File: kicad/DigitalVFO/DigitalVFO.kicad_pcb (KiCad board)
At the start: 2 copper layers, 86.1 x 56.5 mm, 41 parts, among them J1 Coax, J2 Conn_01x03, Q1 2N2222A, SW1 Rotary_Encoder_Switch, U1 74HC14, U2 Teensy3.2, U3 LCD1602A, U4 DDS-60

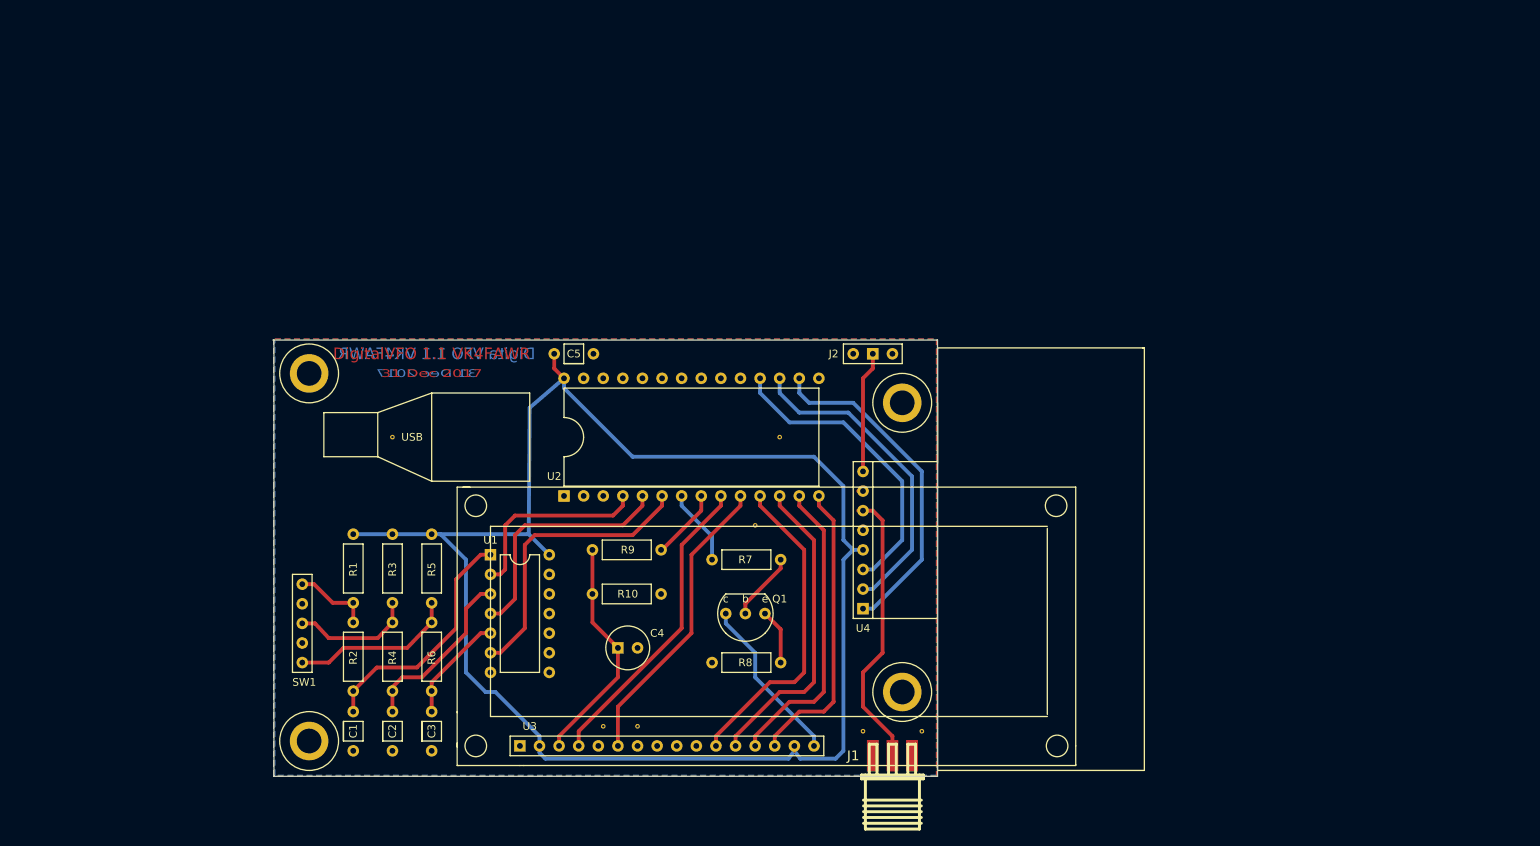
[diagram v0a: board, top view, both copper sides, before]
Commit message: Changing footprints and smaller board
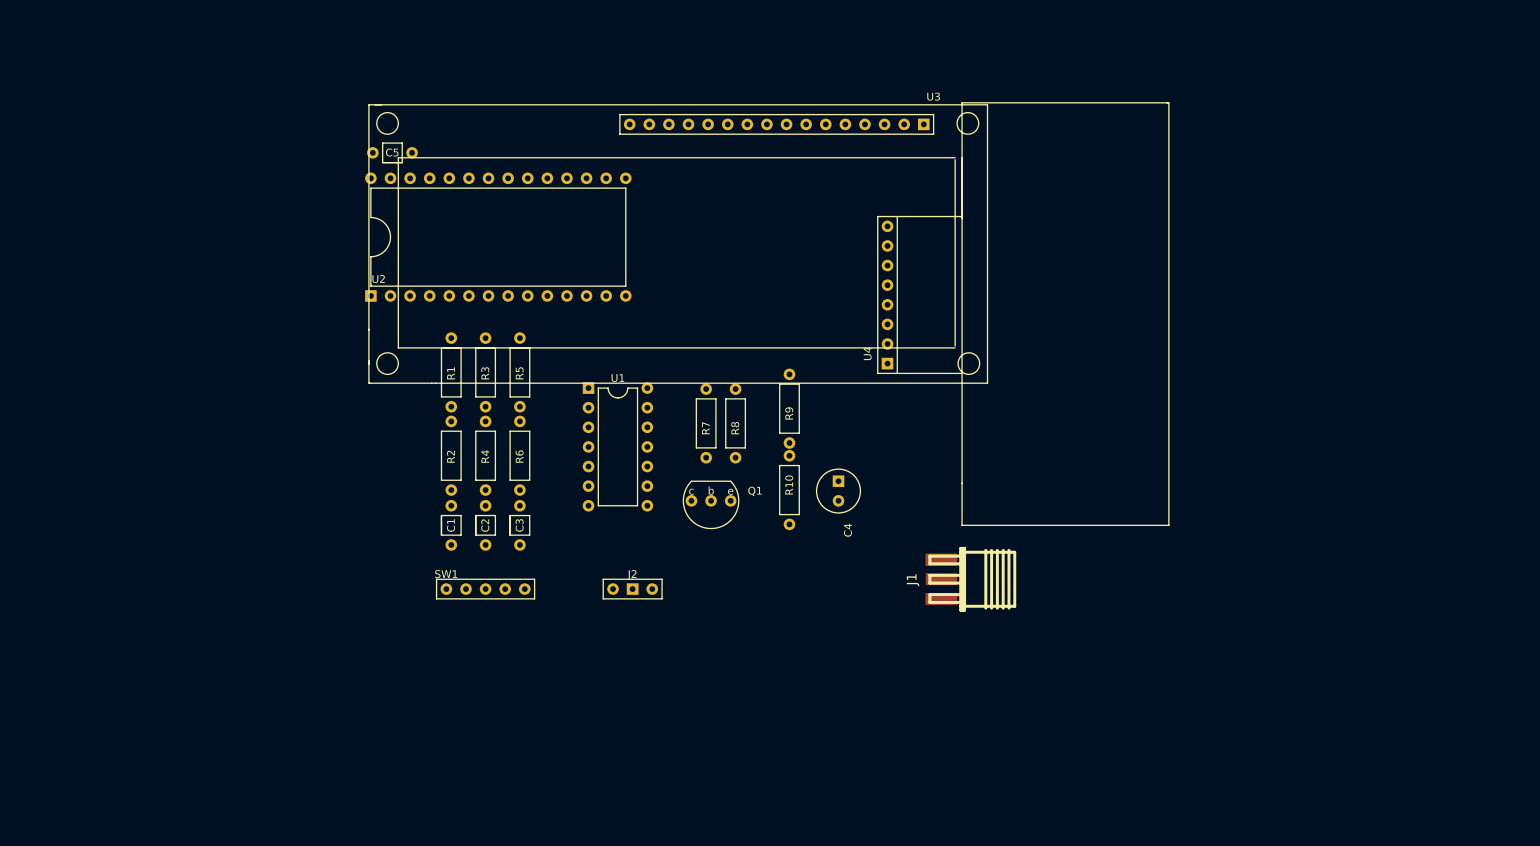
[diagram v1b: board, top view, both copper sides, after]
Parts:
- removed REF** (x14): Via-0.6mm, teensy:Via-0.6mm
- removed REF** (x4): Conn_Mount, teensy:Conn_Mount
- moved U3 50.8 mm to (135.9, 64.1)
- moved J2 43.6 mm to (142.9, 93.3)
- moved C4 35.8 mm to (169.5, 79.4), turned to 270 degrees
- moved U2 35.5 mm to (126.4, 47.6), turned to 0 degrees
- moved C5 35.1 mm to (109.2, 36.8)
- moved U4 31.9 mm to (175.9, 55.2)
- moved R8 31.1 mm to (156.2, 71.8), turned to 90 degrees
- moved C1 29.5 mm to (119.4, 82.5)
- moved C2 29.3 mm to (123.8, 82.5)
- moved C3 29.0 mm to (128.3, 82.5)
- moved R2 29.0 mm to (119.4, 76.2)
- moved R4 28.7 mm to (123.8, 76.2)
- moved R6 28.4 mm to (128.3, 76.2)
- moved R1 28.4 mm to (119.4, 65.4)
- moved R3 28.1 mm to (123.8, 65.4)
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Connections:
- U2 pad 4: Net-(U1-Pad2) -> Net-(U1-Pad6)
- U2 pad 6: Net-(U1-Pad6) -> Net-(U1-Pad2)
- U3 pad 11: Net-(U2-Pad11) -> Net-(U2-Pad12)
- U3 pad 12: Net-(U2-Pad12) -> Net-(U2-Pad11)
- U3 pad 13: Net-(U2-Pad13) -> Net-(U2-Pad10)
- U3 pad 14: Net-(U2-Pad14) -> Net-(U2-Pad9)
- U3 pad 4: Net-(U2-Pad9) -> Net-(U2-Pad14)
- U3 pad 6: Net-(U2-Pad10) -> Net-(U2-Pad13)
- U4 pad 1: Net-(U2-Pad16) -> Net-(U2-Pad18)
- U4 pad 3: Net-(U2-Pad18) -> Net-(U2-Pad16)
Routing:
- net +5V: track 210.3 -> 0.00 mm
- net Net-(U2-Pad16): track 43.7 -> 0.00 mm
- net Net-(U2-Pad11): track 42.0 -> 0.00 mm
- net Net-(U2-Pad17): track 41.5 -> 0.00 mm
- net Net-(U2-Pad12): track 40.5 -> 0.00 mm
- net Net-(U2-Pad9): track 40.0 -> 0.00 mm
- net Net-(U2-Pad18): track 40.0 -> 0.00 mm
- net Net-(U2-Pad13): track 39.9 -> 0.00 mm
- net Net-(U2-Pad10): track 39.0 -> 0.00 mm
- net Net-(U2-Pad14): track 38.2 -> 0.00 mm
- net Net-(U1-Pad6): track 37.7 -> 0.00 mm
- net Net-(J1-Pad1): track 37.4 -> 0.00 mm
- net Net-(C1-Pad1): track 32.0 -> 0.00 mm
- net Net-(U1-Pad4): track 31.6 -> 0.00 mm
- net Net-(C4-Pad1): track 29.9 -> 0.00 mm
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- removed copper zone on B.Cu, net GND
- removed copper zone on F.Cu, net GND
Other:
- board outline removed
- net class normal removed
- board text removed: "31 Dec 2017"
- board text removed: "DigitalVFO 1.1 VK4FAWR"

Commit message: Working on new PCB
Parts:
- J1: footprint teensy:Conn_SMA_Edge -> Connectors:SMA_THT_Jack_Straight
- moved J1 91.8 mm to (95.9, 69.2), turned to 180 degrees
- moved U4 76.3 mm to (99.7, 50.8), turned to 180 degrees
- moved C5 52.5 mm to (160.0, 50.2), turned to 180 degrees
- moved U3 46.7 mm to (90.2, 54.6)
- moved U1 23.6 mm to (131.4, 53.3), turned to 90 degrees
- moved C3 23.0 mm to (117.5, 62.2)
- moved R5 23.0 mm to (117.5, 45.1)
- moved R6 23.0 mm to (117.5, 55.9)
- moved C1 23.0 mm to (108.6, 62.2)
- moved C2 23.0 mm to (113.0, 62.2)
- moved R1 23.0 mm to (108.6, 45.1)
- moved R2 23.0 mm to (108.6, 55.9)
- moved R3 23.0 mm to (113.0, 45.1)
- moved R4 23.0 mm to (113.0, 55.9)
- moved J2 21.9 mm to (132.1, 74.3)
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
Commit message: Almost ready with v1.2
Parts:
- added C6: 0.1uF, teensy:Cap_SmV, F.Cu at (168.1, 90.9)
- added C7: 0.1uF, teensy:Cap_SmV, F.Cu at (162.6, 106.2)
- added G***: LOGO, teensy:logo, F.Cu at (147.8, 80.8)
- added REF**: Conn_Mount, teensy:Conn_Mount, F.Cu at (235.7, 68.1)
- added REF**: Conn_Mount, teensy:Conn_Mount, F.Cu at (144.3, 68.1)
- added REF**: Conn_Mount, teensy:Conn_Mount, F.Cu at (144.3, 109.7)
- added REF**: Conn_Mount, teensy:Conn_Mount, F.Cu at (219.5, 105.7)
- added REF**: Via-0.6mm, teensy:Via-0.6mm, F.Cu at (234.2, 77.7)
- added STRAP**: Strap_23, teensy:Strap_23, F.Cu at (159.0, 94.0)
- J1: footprint Connectors:SMA_THT_Jack_Straight -> teensy:BNC_Socket
- J2: value Conn_01x03 -> Conn_01x02; footprint teensy:Conn_Power_3 -> teensy:Conn_Power_2
- SW1: footprint teensy:Conn_RE5 -> teensy:Conn_RE_Switch
- moved J1 143.0 mm to (233.7, 107.3), turned to 270 degrees
- moved U2 89.2 mm to (221.0, 81.3)
- moved C5 88.7 mm to (238.3, 91.9)
- moved U3 88.6 mm to (167.6, 97.5)
- moved SW1 85.6 mm to (194.1, 103.6), turned to 0 degrees
- moved R7 82.9 mm to (217.9, 92.5), turned to 0 degrees
- moved R8 81.1 mm to (217.9, 97.0), turned to 0 degrees
- moved U4 78.4 mm to (165.1, 94.0)
- moved C3 74.5 mm to (181.5, 100.3)
- moved C2 74.3 mm to (176.8, 100.3)
- moved R6 74.2 mm to (181.5, 93.3)
- moved C1 74.1 mm to (172.1, 100.3)
- moved R4 73.9 mm to (176.8, 93.3)
- moved R5 73.8 mm to (181.5, 81.9)
- moved R2 73.7 mm to (172.1, 93.3)
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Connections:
- J2 pad 1: GND -> Net-(C7-Pad1)
- J2 pad 2: Net-(J2-Pad2) -> GND
- U2 pad 22: (no net) -> Net-(R7-Pad2)
- U2 pad 7: Net-(R7-Pad2) -> (no net)
- U3 pad 11: Net-(U2-Pad12) -> Net-(U2-Pad11)
- U3 pad 12: Net-(U2-Pad11) -> Net-(U2-Pad12)
- U3 pad 13: Net-(U2-Pad10) -> Net-(U2-Pad13)
- U3 pad 14: Net-(U2-Pad9) -> Net-(U2-Pad14)
- U3 pad 4: Net-(U2-Pad14) -> Net-(U2-Pad9)
- U3 pad 6: Net-(U2-Pad13) -> Net-(U2-Pad10)
- U4 pad 8: Net-(J2-Pad2) -> Net-(C7-Pad1)
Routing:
- net +5V: track 0.00 -> 120.6 mm
- net Net-(J1-Pad1): track 0.00 -> 80.8 mm
- net Net-(Q1-Pad3): track 0.00 -> 55.8 mm, vias 0 -> 2
- net Net-(C4-Pad1): track 0.00 -> 55.3 mm, vias 0 -> 1
- net Net-(U2-Pad18): track 0.00 -> 53.4 mm
- net Net-(U2-Pad17): track 0.00 -> 52.0 mm
- net Net-(U2-Pad16): track 0.00 -> 49.8 mm
- net Net-(U1-Pad2): track 0.00 -> 43.8 mm, vias 0 -> 1
- net Net-(U1-Pad4): track 0.00 -> 40.7 mm, vias 0 -> 1
- net Net-(U1-Pad6): track 0.00 -> 37.5 mm, vias 0 -> 1
- net Net-(U2-Pad14): track 0.00 -> 32.1 mm
- net Net-(U2-Pad13): track 0.00 -> 31.5 mm
- net Net-(U2-Pad12): track 0.00 -> 30.9 mm
- net Net-(R9-Pad2): track 0.00 -> 30.8 mm, vias 0 -> 1
- net Net-(R3-Pad2): track 0.00 -> 30.8 mm
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- added copper zone on B.Cu, net GND
- added copper zone on F.Cu, net GND
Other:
- board outline added: 99.6 x 49.8 mm
- net class Default: trace_width 0.25 -> 0.5
- board text added: "DigitalVFO 1.2 VK4FAWR 17 Mar 2561"

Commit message: Final version?
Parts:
- added D1: 1N4001, teensy:Diode_SmH, F.Cu at (163.1, 109.7)
- added J3: Conn_01x02, teensy:Conn_Power_2, F.Cu at (189.5, 109.7)
- added R11: 0R0, teensy:Res_SmH, F.Cu at (180.3, 109.7)
- added REF**: Conn_Mount, teensy:Conn_Mount, F.Cu at (162.6, 75.2)
- moved REF** 8.41 mm to (211.8, 102.1)
- moved SW1 6.60 mm to (200.7, 103.6)
- moved J2 6.12 mm to (171.2, 109.7)
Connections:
- J2 pad 1: Net-(C7-Pad1) -> Net-(D1-Pad2)
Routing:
- net +5V: track 120.6 -> 142.7 mm
- net Net-(R5-Pad2): track 28.1 -> 33.3 mm
- net Net-(R1-Pad2): track 30.6 -> 35.5 mm
- net Net-(J1-Pad1): track 80.8 -> 77.1 mm
- net Net-(J3-Pad1): track 0.00 -> 3.30 mm
- net Net-(R3-Pad2): track 30.8 -> 34.1 mm
- net Net-(D1-Pad2): track 0.00 -> 2.54 mm
- net Net-(C7-Pad1): track 8.94 -> 9.89 mm
- net Net-(Q1-Pad3): track 55.8 -> 54.9 mm
